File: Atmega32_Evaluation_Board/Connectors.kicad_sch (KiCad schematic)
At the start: 9 parts, among them J2 ICSP

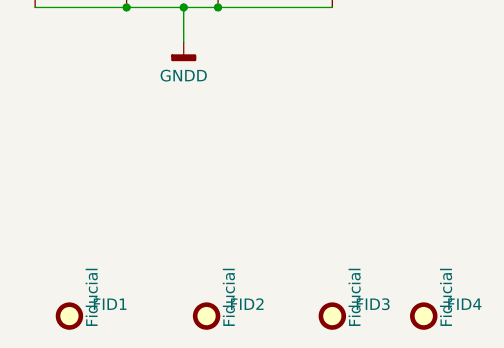
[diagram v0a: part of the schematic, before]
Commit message: added Atmega project
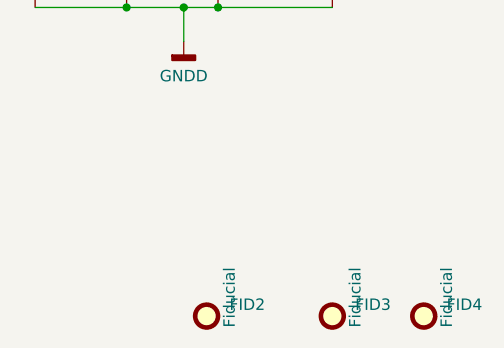
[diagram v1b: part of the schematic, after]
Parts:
- removed FID1: Fiducial, Fiducial:Fiducial_0.75mm_Mask2.25mm, symbol Mechanical:Fiducial
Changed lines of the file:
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@@
-	)
-	(symbol
-		(lib_id "Mechanical:Fiducial")
-		(at 129.54 107.95 0)
-		(unit 1)
-		(exclude_from_sim no)
-		(in_bom no)
-		(on_board yes)
-		(dnp no)
-		(property "Reference" "FID1"
-			(at 132.08 106.6799 0)
-			(effects
-				(font
-					(size 1.27 1.27)
-				)
-				(justify left)
-			)
-		)
-		(property "Value" "Fiducial"
-			(at 132.08 109.2199 90)
-			(effects
-				(font
-					(size 1.27 1.27)
-				)
-				(justify left)
-			)
-		)
-		(property "Footprint" "Fiducial:Fiducial_0.75mm_Mask2.25mm"
-			(at 129.54 107.95 0)
-			(effects
-				(font
-					(size 1.27 1.27)
-				)
-				(hide yes)
-			)
-		)
-		(property "Datasheet" "~"
-			(at 129.54 107.95 0)
-			(effects
-				(font
-					(size 1.27 1.27)
-				)
-				(hide yes)
-			)
-		)
-		(property "Description" "Fiducial Marker"
-			(at 129.54 107.95 0)
-			(effects
-				(font
-					(size 1.27 1.27)
-				)
-				(hide yes)
-			)
-		)
-		(instances
-			(project ""
-				(path "/6c4a903a-5b2c-4fff-b670-18618cb937b9/160c6ff6-4897-4348-9a8b-93014dc18887"
-					(reference "FID1")
-					(unit 1)
-				)
-			)
-		)
 	)
 	(symbol
